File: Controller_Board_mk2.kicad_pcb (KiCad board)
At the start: 2 copper layers, 44 parts, among them J1 Barrel_Jack_MountingPin, J2 Barrel_Jack_MountingPin, J3 Barrel_Jack_MountingPin, J4 Barrel_Jack_MountingPin, J5 Barrel_Jack_MountingPin, K1 SANYOU_SRD_Form_C, K2 SANYOU_SRD_Form_C, K3 SANYOU_SRD_Form_C, K4 SANYOU_SRD_Form_C, Q1 BC817, Q2 BC817, Q3 BC817, Q4 BC817, U1 AP63205WU

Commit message: minor trace fixes
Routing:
- net Net-(D1-K): track 295.4 -> 302.4 mm
- net Net-(U1-EN): track 20.6 -> 19.9 mm

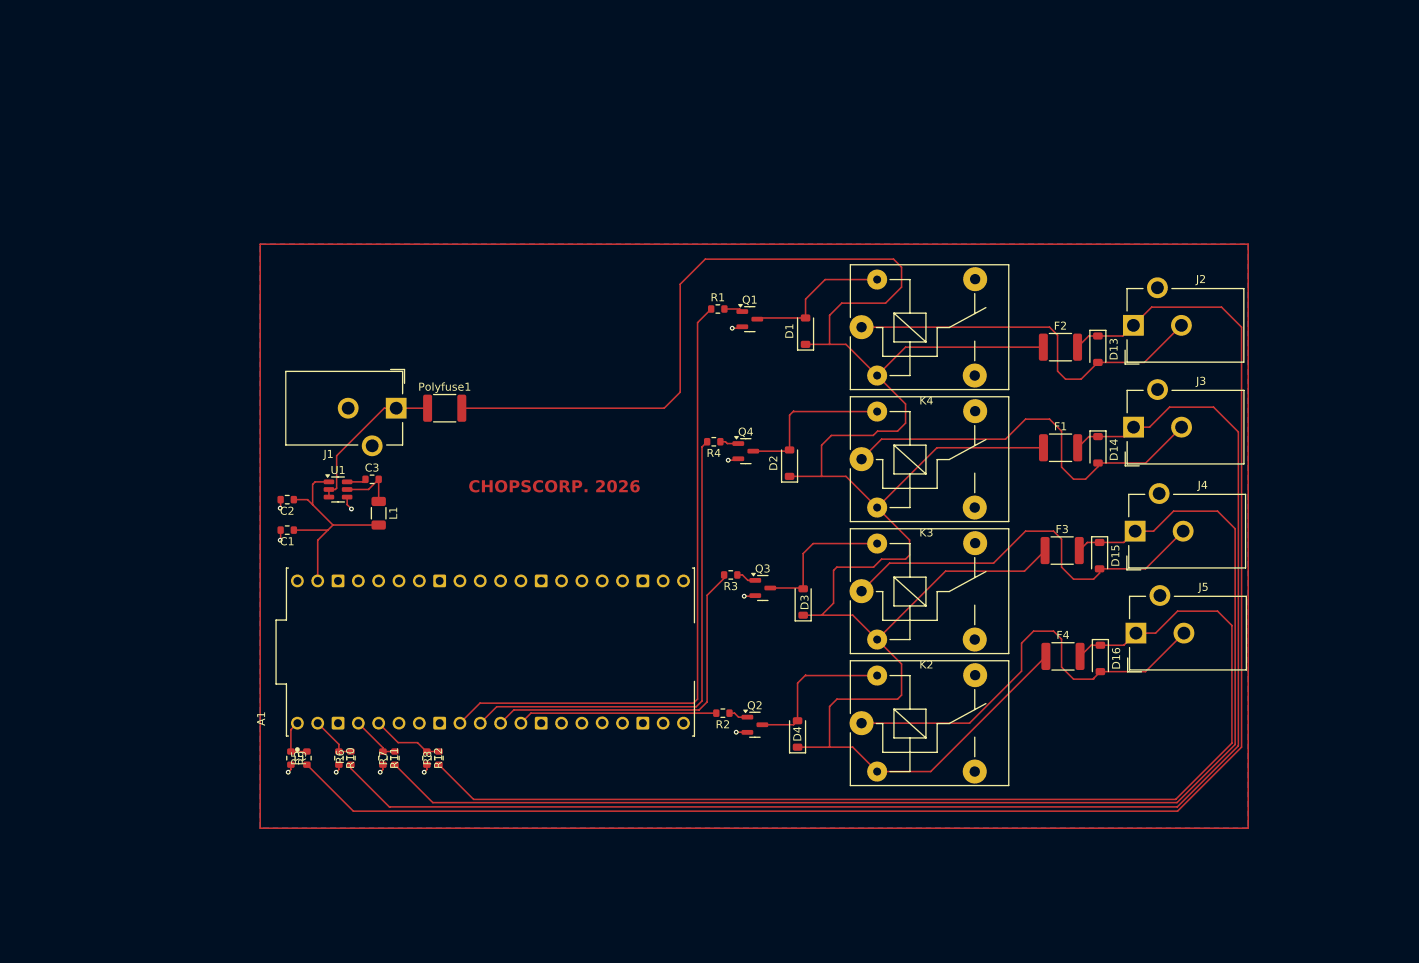
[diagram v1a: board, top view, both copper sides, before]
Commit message: added through holes, reworked copper pour and edge cuts.
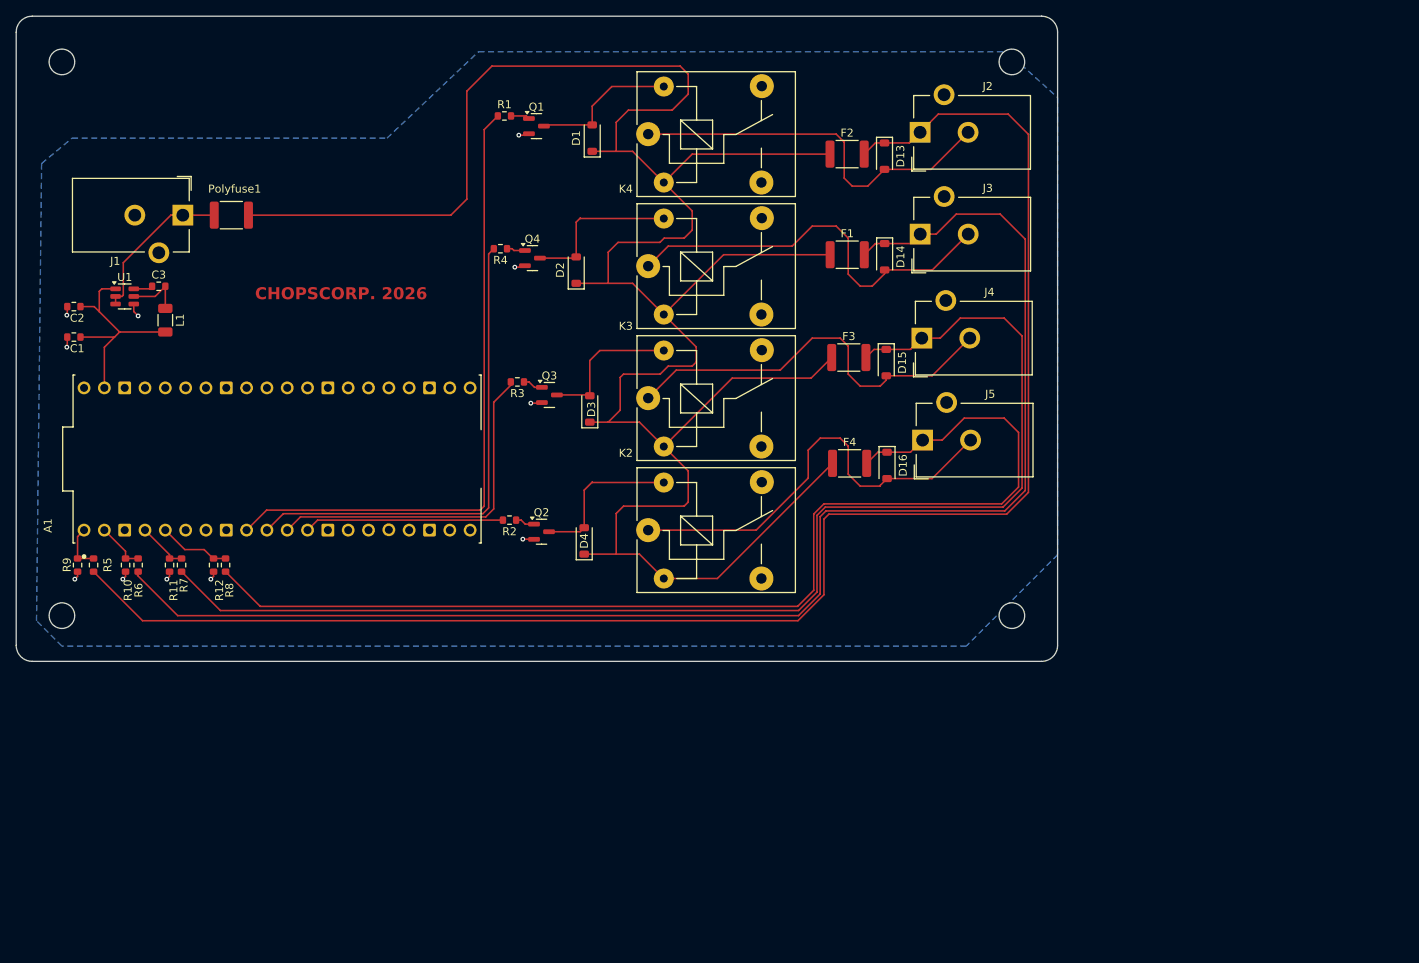
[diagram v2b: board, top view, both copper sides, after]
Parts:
- added REF**: MountingHole_3.2mm_M3, MountingHole:MountingHole_3.2mm_M3, F.Cu at (5.71, 74.9)
- added REF**: MountingHole_3.2mm_M3, MountingHole:MountingHole_3.2mm_M3, F.Cu at (124.5, 74.9)
- added REF**: MountingHole_3.2mm_M3, MountingHole:MountingHole_3.2mm_M3, F.Cu at (5.71, 5.71)
- added REF**: MountingHole_3.2mm_M3, MountingHole:MountingHole_3.2mm_M3, F.Cu at (124.5, 5.71)
- moved D15 36.0 mm to (108.8, 43.3)
- moved F1 36.0 mm to (103.9, 29.8)
- moved K1 36.0 mm to (79.0, 64.2)
- moved A1 36.0 mm to (32.6, 55.4)
- moved C1 36.0 mm to (7.21, 40.1)
- moved C2 36.0 mm to (7.21, 36.3)
- moved C3 36.0 mm to (17.8, 33.8)
- moved D1 36.0 mm to (72.0, 15.2)
- moved D13 36.0 mm to (108.5, 17.5)
- moved D16 36.0 mm to (108.9, 56.1)
- moved D2 36.0 mm to (70.0, 31.7)
- moved D3 36.0 mm to (71.7, 49.1)
- moved D4 36.0 mm to (71.0, 65.6)
- moved F2 36.0 mm to (103.9, 17.2)
- moved F3 36.0 mm to (104.1, 42.7)
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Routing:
- net Net-(D13-K): track 198.7 -> 200.0 mm
- net Net-(D14-K): track 180.9 -> 182.2 mm
- net Net-(D15-K): track 159.4 -> 160.5 mm
- net Net-(D16-K): track 140.6 -> 141.6 mm
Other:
- board outline added: 130.2 x 80.6 mm

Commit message: minor fixes
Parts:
- moved A1 56.0 mm to (75.8, 91.0)
- moved D14 56.0 mm to (151.7, 65.7)
- moved D2 56.0 mm to (113.2, 67.4)
- moved K1 56.0 mm to (122.2, 99.9)
- moved K2 56.0 mm to (122.2, 83.4)
- moved K3 56.0 mm to (122.2, 66.9)
- moved C1 56.0 mm to (50.4, 75.7)
- moved C2 56.0 mm to (50.4, 71.9)
- moved D1 56.0 mm to (115.2, 50.9)
- moved D15 56.0 mm to (151.9, 78.9)
- moved D4 56.0 mm to (114.2, 101.2)
- moved F1 56.0 mm to (147.1, 65.4)
- moved J1 56.0 mm to (64.0, 60.5)
- moved J3 56.0 mm to (156.2, 62.9)
- moved K4 56.0 mm to (122.2, 50.4)
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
